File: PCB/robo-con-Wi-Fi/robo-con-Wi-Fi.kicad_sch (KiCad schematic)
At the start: 120 parts, among them J1 Conn_01x04, J2 SMA-J, J3 Conn_01x05, J4 Conn_01x01, J5 Conn_01x02, J6 Conn_01x01, J7 Conn_01x06, Q1 2SC3325-Y, SW1 SW_Push, SW2 SW_Push, U1 STM32H723VGTx, U10 MCP73831-2-OT, U11 LM66100DCK, U12 NJM12877, U13 TXB0606DYYR, U14 TPS628513DRLR, U15 LM66100DCK, U18 USB_Type-C, U2 LBEE5HY2FY, U3 TXU0204, U5 RKJXV122400R, U6 IS25LP064D-JLLE, U7 RKJXV122400R, U8 TMHU28, U9 TMHU28, Y2 XRCGB25M000FFS1AR0

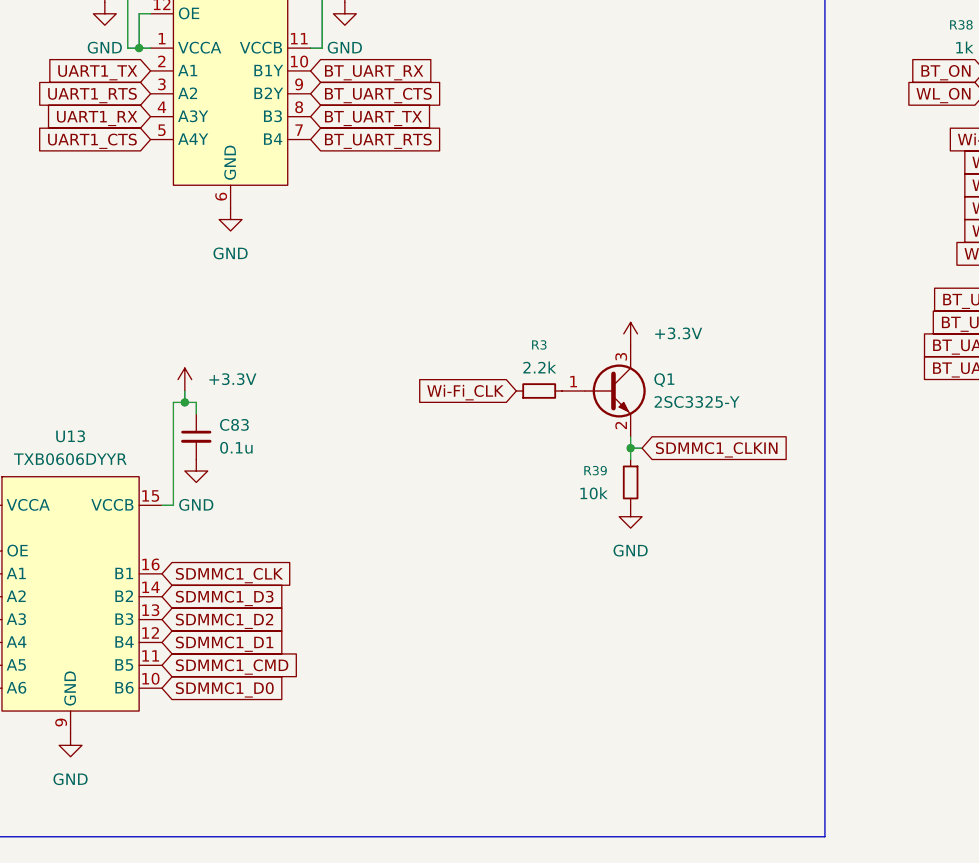
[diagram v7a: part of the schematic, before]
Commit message: sdioのプルアップ追加
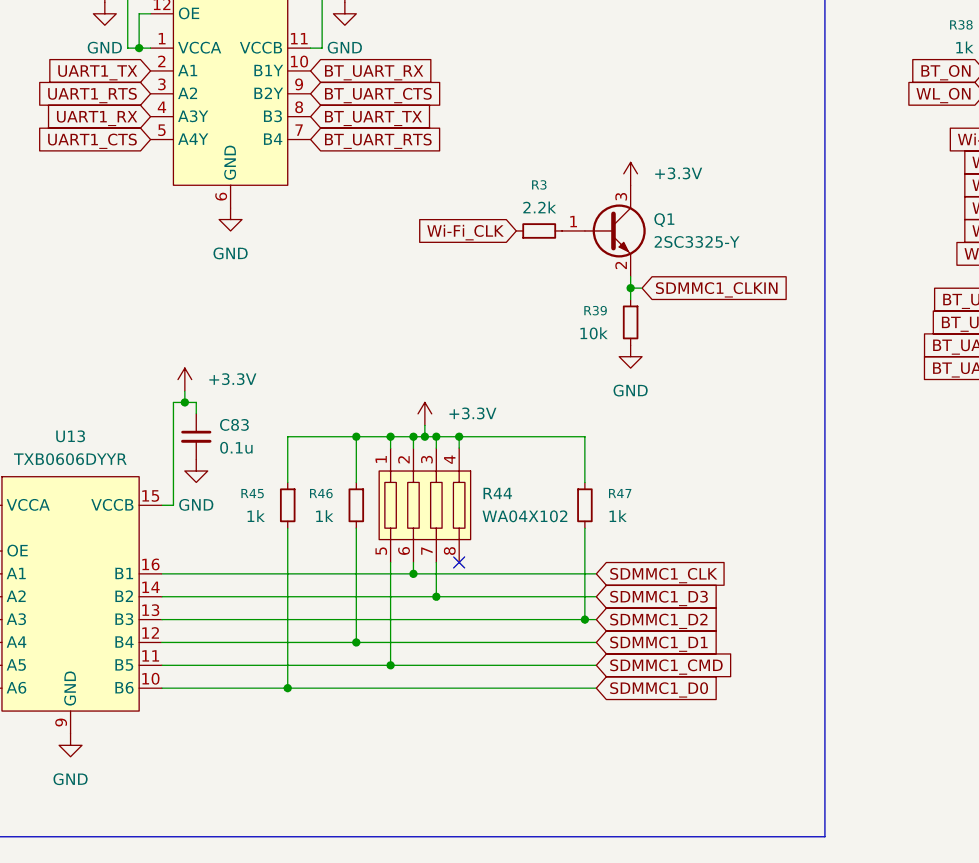
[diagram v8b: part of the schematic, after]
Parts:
- added R44: WA04X102, My_Library:WA04X102, symbol My_Library:WA04X102
- added R45, R46, R47: 1k, Resistor_SMD:R_0402_1005Metric_Pad0.72x0.64mm_HandSolder, symbol Device:R_Small
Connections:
- net +3.3V: now also R44.1, R44.2, R44.3, R44.4, R45.1, R46.1, R47.1
- net SDMMC1_CLK: now also R44.6
- net SDMMC1_CMD: now also R44.5
- net SDMMC1_D0: now also R45.2
- net SDMMC1_D1: now also R46.2
- net SDMMC1_D2: now also R47.2
- net SDMMC1_D3: now also R44.7
- no-connect marks 51 -> 52
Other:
- moved on the sheet: Q1, R3, R39
